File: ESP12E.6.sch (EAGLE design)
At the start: 50 parts, among them CN2 1X4-BIG, J1 1X2-3.5MM, J4 1X2-3.5MM, U1 A5984-TSSOP, U2 SPX3819M5-L-3-3

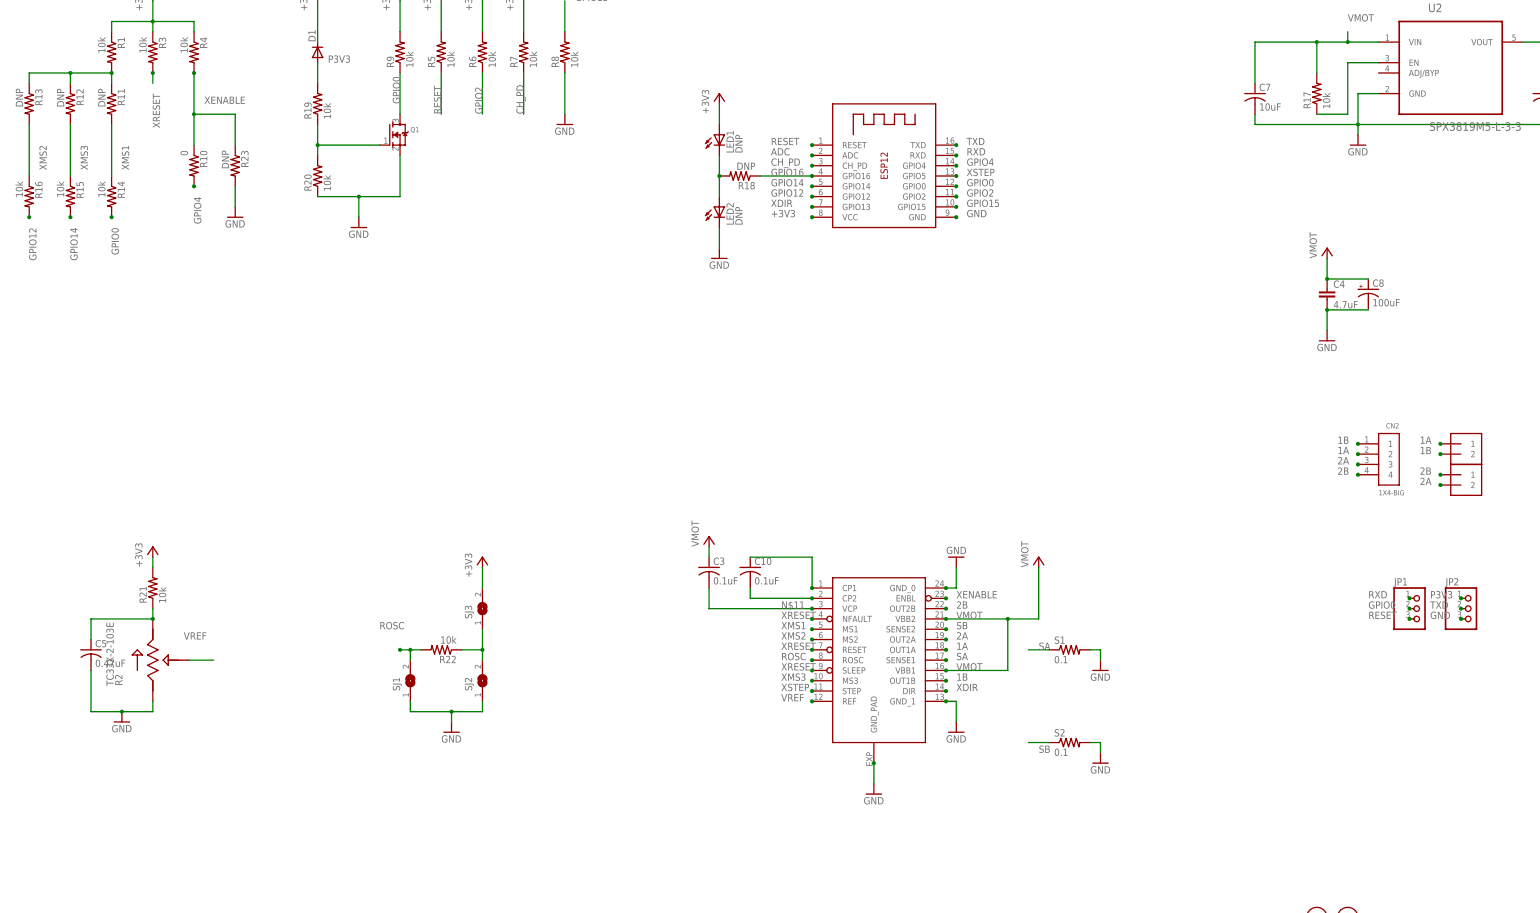
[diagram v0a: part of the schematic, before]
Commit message: GPIO pins repurposed
GPIO 12 and 14 broken out to to pin headers for general use. Required
that the MS section of board to be modified. GPIO0 now can control step
mode between 0 and 32 micro-stepping.
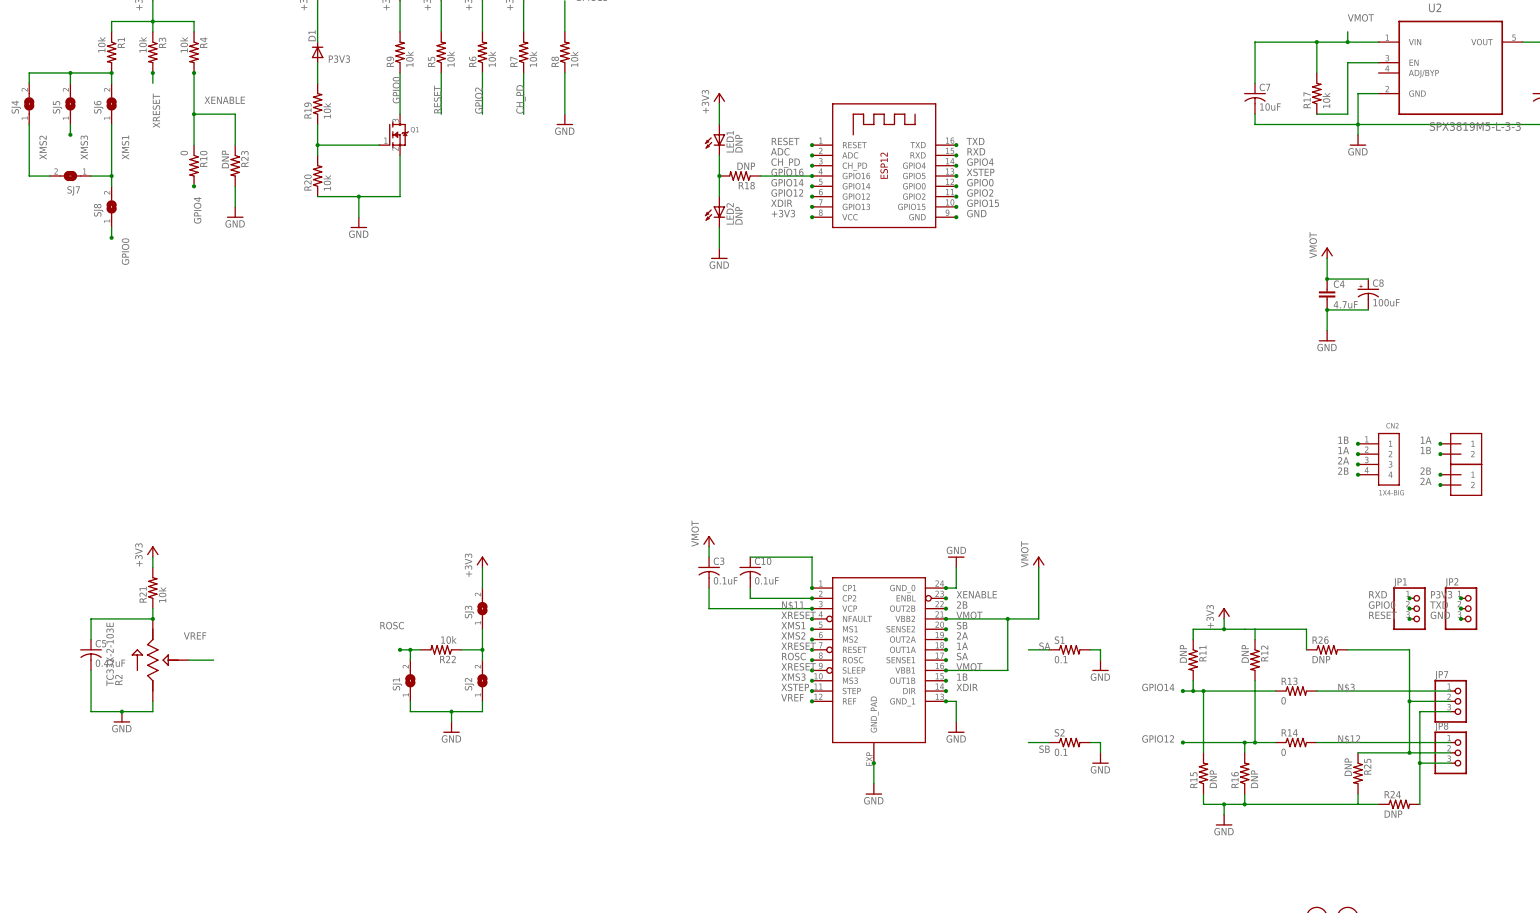
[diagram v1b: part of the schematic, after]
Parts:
- added JP7, JP8: (no value), adafruit:PINHD-1X3
- added R24, R25, R26: DNP, adafruit:R-US_R0603
- added SJ4, SJ5, SJ6, SJ7, SJ8: (no value), jumper:SJ
- R13: value DNP -> 0
- R14: value 10k -> 0
- R15, R16: value 10k -> DNP
- U1: value A5984-TSSOP -> A5984
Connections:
- new net N$10: JP7.2, JP8.2, R25.1, R26.2
- new net N$12: JP8.1, R14.2
- new net N$3: JP7.1, R13.2
- new net N$9: JP7.3, JP8.3, R24.2
- net +3V3: now also R11.1, R12.1, R26.1
- net GND: now also R15.1, R16.1, R24.1, R25.2
- net GPIO0: now also SJ8.1; no longer R14.2
- net GPIO12: now also R12.2, R14.1
- net GPIO14: now also R11.2, R13.1
- net MSN: now also SJ4.2, SJ5.2, SJ6.2; no longer R11.1, R12.1, R13.1
- net XMS1: now also SJ6.1, SJ7.1, SJ8.2; no longer R11.2, R14.1
- net XMS2: now also SJ4.1, SJ7.2; no longer R13.2, R16.1
- net XMS3: now also SJ5.1; no longer R12.2, R15.1
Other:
- moved on the sheet: R11, R12, R13, R14, R15, R16

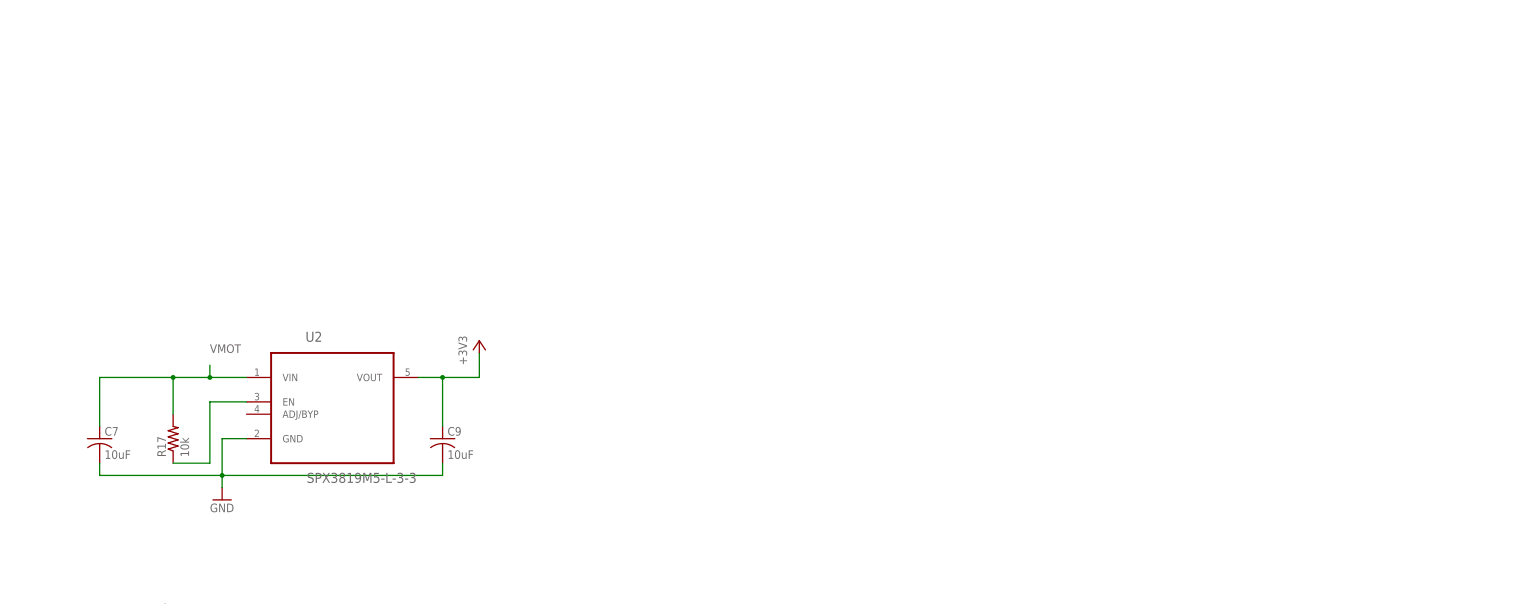
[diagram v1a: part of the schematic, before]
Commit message: Buck Regulator
Prototype +3.3V DC buck regultaor. Based around TI TPS62177 IC.
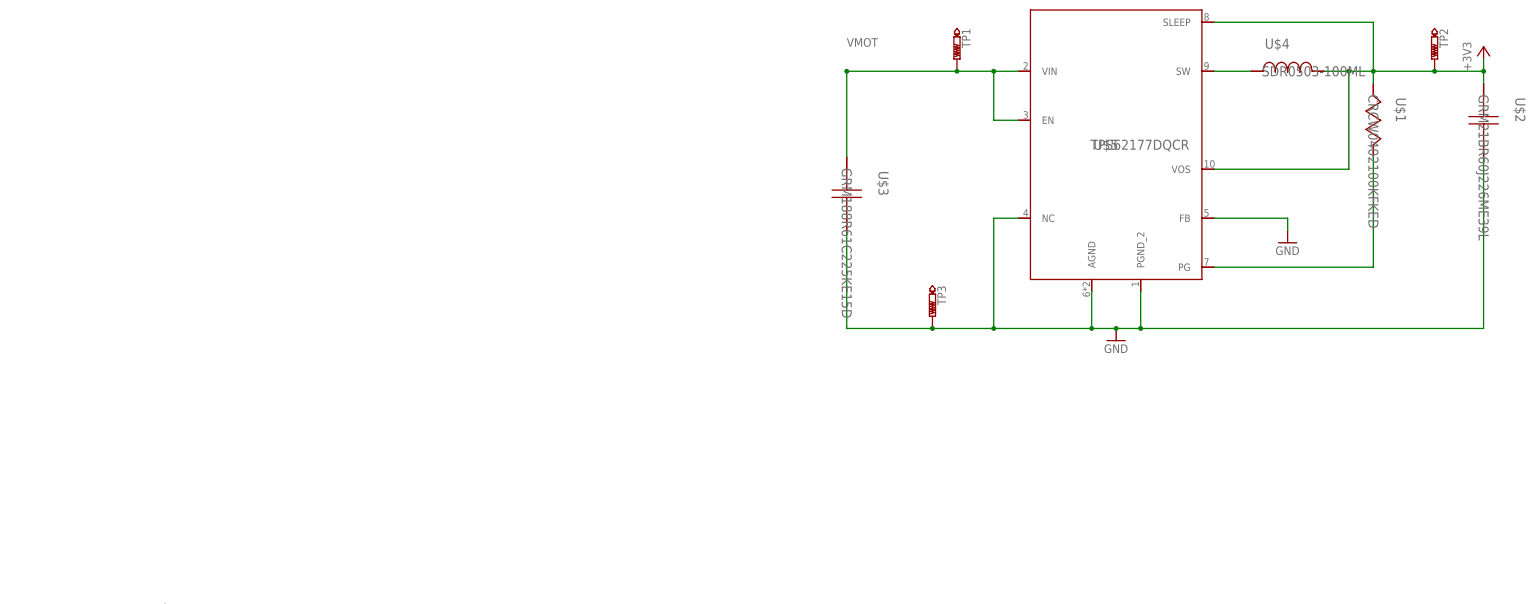
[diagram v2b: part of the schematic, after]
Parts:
- removed C7, C9: 10uF, adafruit:C-USC0603K
- removed R17: 10k, adafruit:R-US_R0603
- removed U2: SPX3819M5-L-3-3, SPX3819M5-L-3-3:SPX3819M5-L-3-3
- added TP1, TP2, TP3: PTR1B1,27, testpad:PTR1B1,27
- added U$1: CRCW0402100KFKED, TPS62177:CRCW0402100KFKED
- added U$2: GRM21BR60J226ME39L, TPS62177:GRM21BR60J226ME39L
- added U$3: GRM188R61C225KE15D, TPS62177:GRM188R61C225KE15D
- added U$4: SDR0503-100ML, TPS62177:SDR0503-100ML
- added U$5: TPS62177DQCR, TPS62177:TPS62177DQCR
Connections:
- removed net N$4: R17.1, U2.EN
- new net N$14: U$1.1, U$5.PG
- new net N$17: U$4.1, U$5.SW
- net +3V3: now also TP2.TP, U$1.2, U$2.2, U$4.2, U$5.SLEEP, U$5.VOS; no longer C9.1, U2.VOUT
- net GND: now also TP3.TP, U$2.1, U$3.1, U$5.AGND, U$5.FB, U$5.NC, U$5.PGND_2; no longer C7.2, C9.2, U2.GND
- net VMOT: now also TP1.TP, U$3.2, U$5.EN, U$5.VIN; no longer C7.1, R17.2, U2.VIN

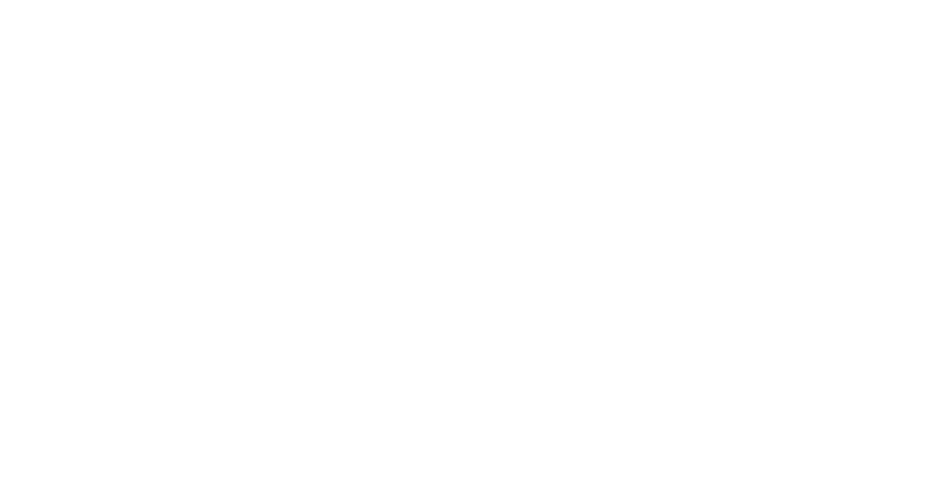
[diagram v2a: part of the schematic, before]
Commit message: License Update
Licensed under CERN OHL v.1.2 or later
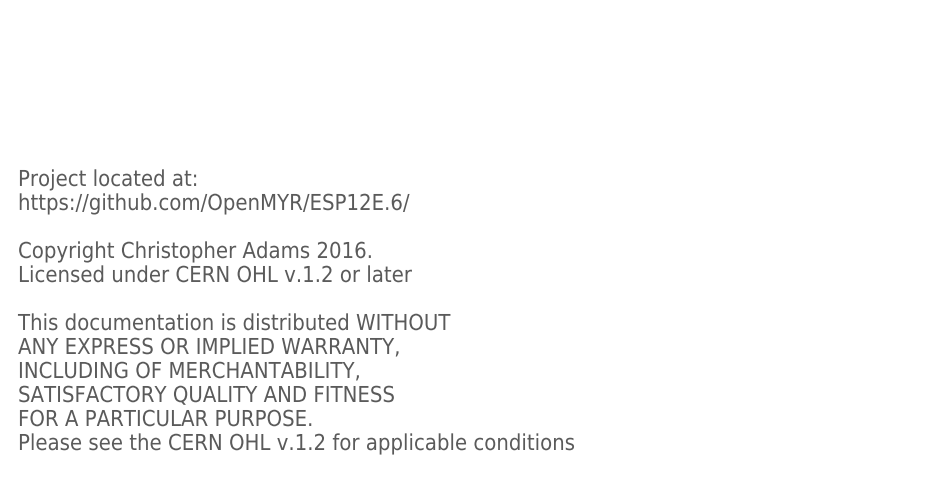
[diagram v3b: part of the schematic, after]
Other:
- note added: "Project located at: https://github.com/OpenMYR/ESP12E.6/ Copyright Christopher Adams 2016. Licensed under CERN OHL v.1.2 or later This documentation is distributed WITHOUT ANY EXPRESS OR IMPLIED WARRANTY, INCLUDING OF MERCHANTABILITY, SATISFACTORY QUALITY AND FITNESS FOR A PARTICULAR PURPOSE. Please see the CERN OHL v.1.2 for applicable conditions"
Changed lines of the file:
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@@
 <sheet>
 <plain>
+<text x="5.08" y="2.54" size="1.778" layer="97">Project located at:
+https://github.com/OpenMYR/ESP12E.6/
+Copyright Christopher Adams 2016.
+Licensed under CERN OHL v.1.2 or later
+This documentation is distributed WITHOUT
+ANY EXPRESS OR IMPLIED WARRANTY,
+INCLUDING OF MERCHANTABILITY,
+SATISFACTORY QUALITY AND FITNESS
+FOR A PARTICULAR PURPOSE.
+Please see the CERN OHL v.1.2 for applicable conditions</text>
 </plain>
 <instances>
@@
 </schematic>
 </drawing>
+<compatibility>
+<note version="6.3" minversion="6.2.2" severity="warning">
+Since Version 6.2.2 text objects can contain more than one line,
+which will not be processed correctly with this version.
+</note>
+</compatibility>
 </eagle>

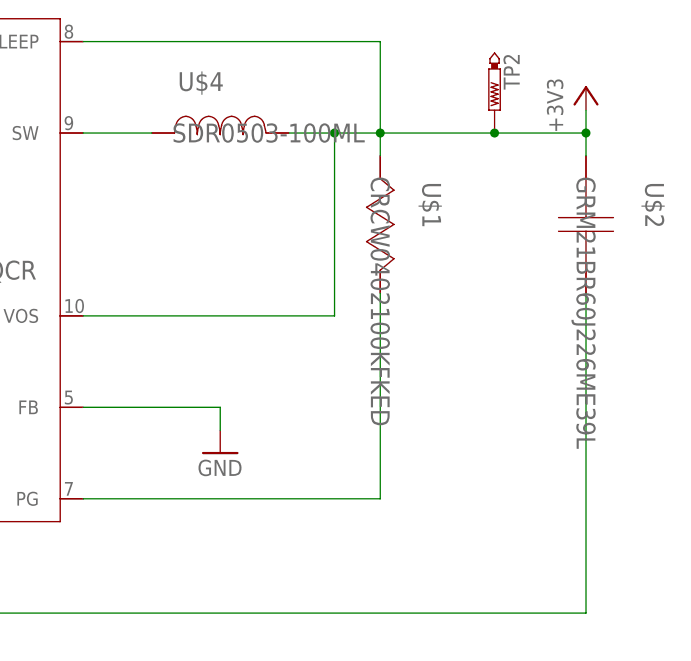
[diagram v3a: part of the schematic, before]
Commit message: Power Isolation
Separation between VMOT/+3V3 and +3V3/GND nets is increased. Rearranged
R3,R21, U$3 and, U$2.
Removed U$1 in the regulator schematic as it was not nessesary.
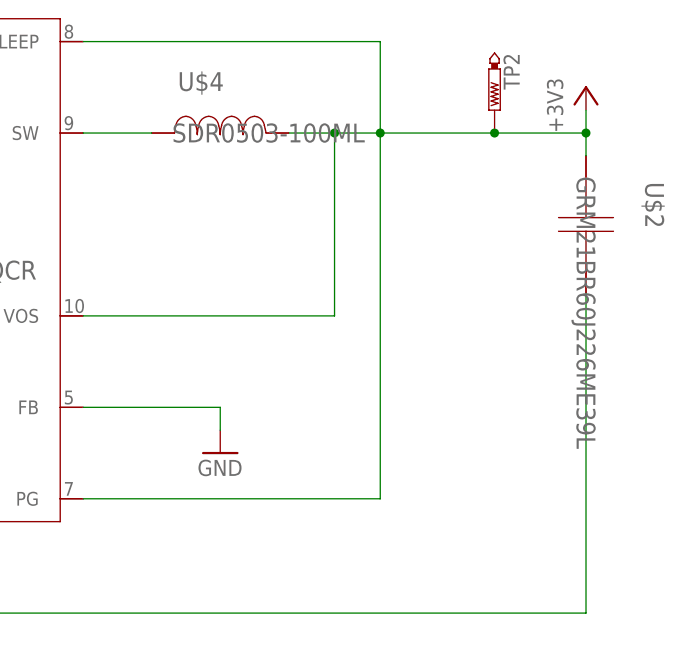
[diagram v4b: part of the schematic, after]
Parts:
- removed U$1: CRCW0402100KFKED, TPS62177:CRCW0402100KFKED
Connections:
- removed net N$14: U$1.1, U$5.PG
- net +3V3: now also U$5.PG; no longer U$1.2
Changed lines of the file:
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@@
 <part name="R25" library="adafruit" deviceset="R-US_" device="R0603" value="DNP"/>
 <part name="R26" library="adafruit" deviceset="R-US_" device="R0603" value="DNP"/>
-<part name="U$1" library="TPS62177" deviceset="CRCW0402100KFKED" device=""/>
 <part name="U$2" library="TPS62177" deviceset="GRM21BR60J226ME39L" device=""/>
 <part name="U$3" library="TPS62177" deviceset="GRM188R61C225KE15D" device=""/>
@@
 <instance part="R25" gate="G$1" x="353.06" y="63.5" rot="R270"/>
 <instance part="R26" gate="G$1" x="345.44" y="93.98"/>
-<instance part="U$1" gate="A" x="591.82" y="297.18" rot="R270"/>
 <instance part="U$2" gate="A" x="614.68" y="297.18" rot="R270"/>
 <instance part="U$3" gate="A" x="482.6" y="281.94" rot="R270"/>
@@
 <pinref part="U$4" gate="A" pin="2"/>
 <wire x1="586.74" y1="307.34" x2="581.66" y2="307.34" width="0.1524" layer="91"/>
-<pinref part="U$1" gate="A" pin="2"/>
-<wire x1="591.82" y1="304.8" x2="591.82" y2="307.34" width="0.1524" layer="91"/>
 <wire x1="591.82" y1="307.34" x2="586.74" y2="307.34" width="0.1524" layer="91"/>
 <junction x="586.74" y="307.34"/>
@@
 <pinref part="TP2" gate="G$1" pin="TP"/>
 <junction x="604.52" y="307.34"/>
+<wire x1="591.82" y1="307.34" x2="591.82" y2="266.7" width="0.1524" layer="91"/>
+<pinref part="U$5" gate="A" pin="PG"/>
+<wire x1="591.82" y1="266.7" x2="558.8" y2="266.7" width="0.1524" layer="91"/>
 </segment>
 </net>
@@
 </segment>
 </net>
-<net name="N$14" class="0">
-<segment>
-<pinref part="U$1" gate="A" pin="1"/>
-<wire x1="591.82" y1="289.56" x2="591.82" y2="266.7" width="0.1524" layer="91"/>
-<pinref part="U$5" gate="A" pin="PG"/>
-<wire x1="591.82" y1="266.7" x2="558.8" y2="266.7" width="0.1524" layer="91"/>
-</segment>
-</net>
